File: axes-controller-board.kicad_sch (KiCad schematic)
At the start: 59 parts, among them IC1 TPS5450QDDARQ1, J10 Conn_01x08, J11 Conn_01x04, J12 Conn_01x08, J13 Conn_01x04, J14 Conn_01x08, J15 Conn_01x08, J16 Conn_01x04, J17 Conn_01x08, J18 Conn_01x08, J19 Conn_01x04, J2 Conn_01x03, J20 Conn_01x08, J21 Conn_01x08, J22 Conn_01x04, J23 Conn_01x08, J24 Conn_01x08, J25 Conn_01x04, J26 Conn_01x08, J27 Raspberry_Pi_2_3, J28 DC1, J29 DC2, J3 Conn_01x03, J30 DC3, J31 Conn_01x08, J32 Conn_01x08, J33 DC1, J4 Conn_01x03, J5 DRIVER, J6 NTC, J7 DRIVER, J8 NTC, J9 Conn_01x08, U1 LM1117MP-3.3

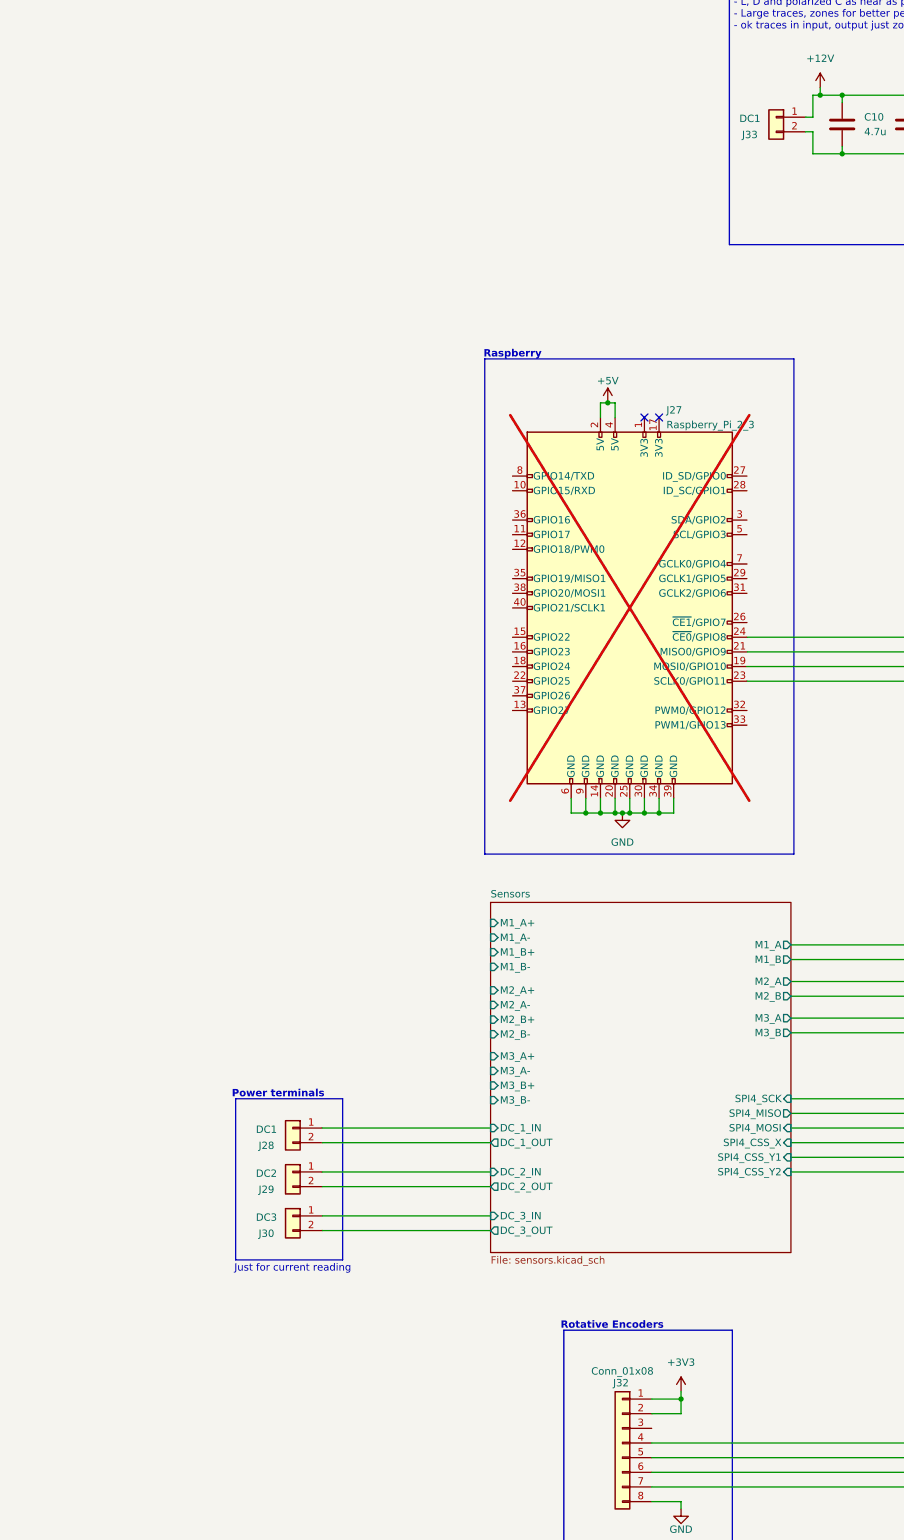
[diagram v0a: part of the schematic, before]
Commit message: fix: connectors and pcb layout
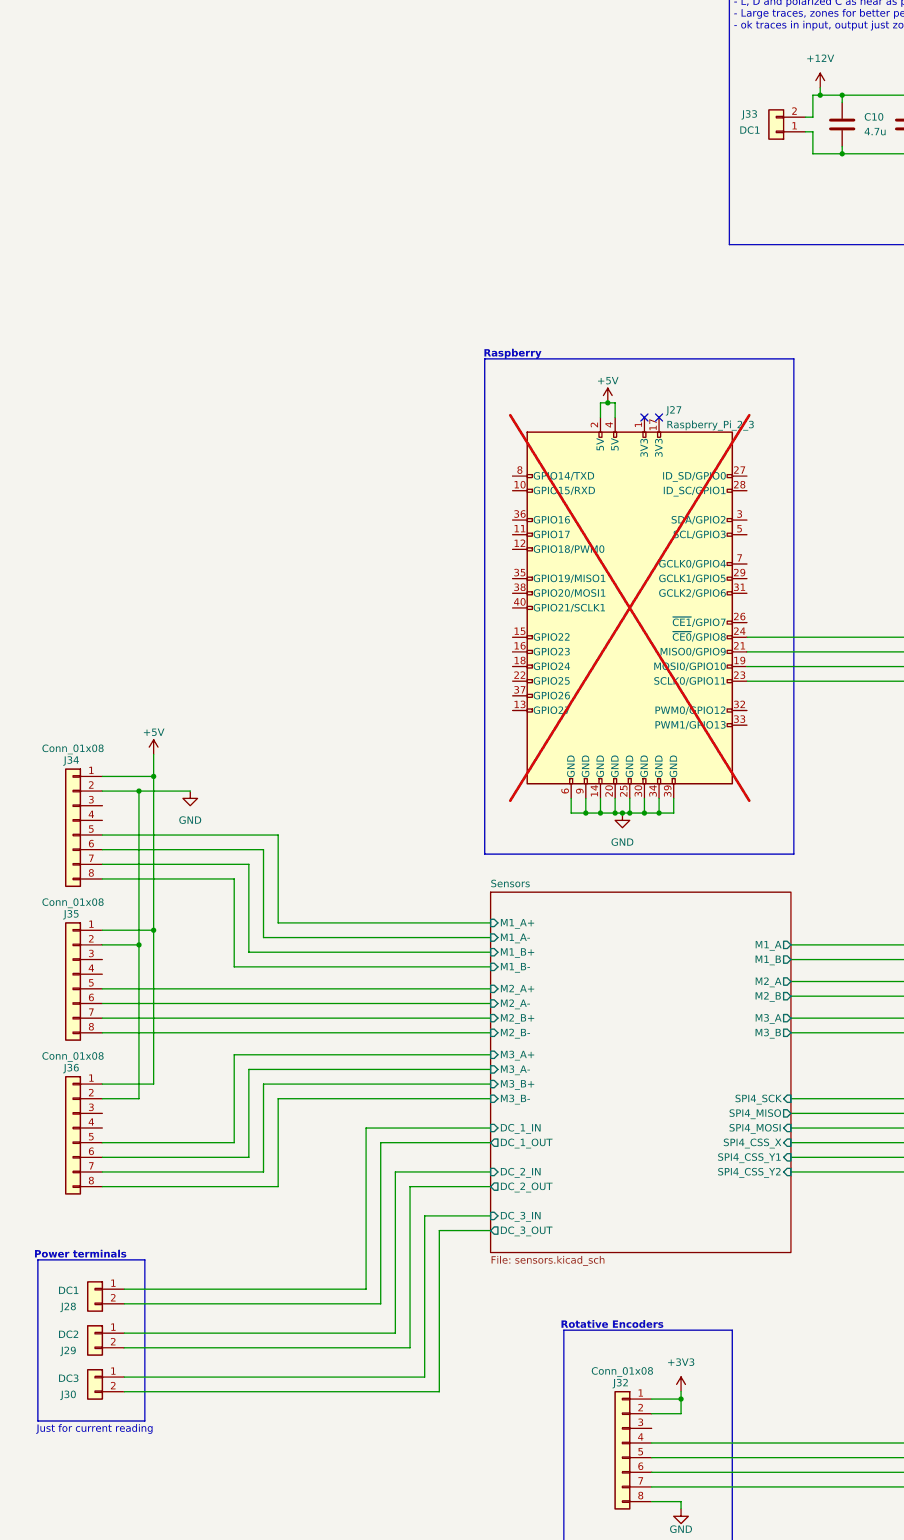
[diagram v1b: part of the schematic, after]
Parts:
- added J34, J35, J36: Conn_01x08, Local:1985250, symbol Connector_Generic:Conn_01x08
- J2, J3, J4: footprint Connector_PinHeader_2.54mm:PinHeader_1x03_P2.54mm_Vertical -> Local:1985205
- J31, J32: footprint Connector_Molex:Molex_Micro-Fit_3.0_43045-0812_2x04_P3.00mm_Vertical -> Local:1985250
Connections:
- net +12V: now also J33.2 (Pin_2); no longer J33.1 (Pin_1)
- net +5V: now also J34.1 (Pin_1), J35.1 (Pin_1), J36.1 (Pin_1)
- net GND: now also J33.1 (Pin_1), J34.2 (Pin_2), J35.2 (Pin_2), J36.2 (Pin_2); no longer J33.2 (Pin_2)
- net Sensors/M1_A+: now also J34.5 (Pin_5)
- net Sensors/M1_A-: now also J34.6 (Pin_6)
- net Sensors/M1_B+: now also J34.7 (Pin_7)
- net Sensors/M1_B-: now also J34.8 (Pin_8)
- net Sensors/M2_A+: now also J35.5 (Pin_5)
- net Sensors/M2_A-: now also J35.6 (Pin_6)
- net Sensors/M2_B+: now also J35.7 (Pin_7)
- net Sensors/M2_B-: now also J35.8 (Pin_8)
- net Sensors/M3_A+: now also J36.5 (Pin_5)
- net Sensors/M3_A-: now also J36.6 (Pin_6)
- net Sensors/M3_B+: now also J36.7 (Pin_7)
- net Sensors/M3_B-: now also J36.8 (Pin_8)
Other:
- moved on the sheet: J28, J29, J30, J33

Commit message: feat: endstops integration
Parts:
- added J37, J38, J39: ENDSTOP, Connector_PinHeader_2.54mm:PinHeader_1x02_P2.54mm_Vertical, symbol Connector_Generic:Conn_01x02
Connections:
- net GND: now also J37.1 (Pin_1), J38.1 (Pin_1), J39.1 (Pin_1)
- new net MCU/ES_X: J37.2 (Pin_2)
- new net MCU/ES_Y1: J38.2 (Pin_2)
- new net MCU/ES_Y2: J39.2 (Pin_2)
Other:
- sheet MCU ports: added ES_X, ES_Y1, ES_Y2; removed none

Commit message: fix: 33R resistors
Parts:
- C51, C52, C53, C54, C55, C56: now not fitted
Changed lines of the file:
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@@
 		(in_bom yes)
 		(on_board yes)
-		(dnp no)
+		(dnp yes)
 		(fields_autoplaced yes)
 		(property "Reference" "C51"
@@
 		(in_bom yes)
 		(on_board yes)
-		(dnp no)
+		(dnp yes)
 		(fields_autoplaced yes)
 		(property "Reference" "C52"
@@
 		(in_bom yes)
 		(on_board yes)
-		(dnp no)
+		(dnp yes)
 		(fields_autoplaced yes)
 		(property "Reference" "C53"
@@
 		(in_bom yes)
 		(on_board yes)
-		(dnp no)
+		(dnp yes)
 		(fields_autoplaced yes)
 		(property "Reference" "C54"
@@
 		(in_bom yes)
 		(on_board yes)
-		(dnp no)
+		(dnp yes)
 		(fields_autoplaced yes)
 		(property "Reference" "C56"
@@
 		(in_bom yes)
 		(on_board yes)
-		(dnp no)
+		(dnp yes)
 		(fields_autoplaced yes)
 		(property "Reference" "C55"

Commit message: feat: spi4 connections
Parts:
- added J40: Conn_01x03, Local:1985205, symbol Connector_Generic:Conn_01x03
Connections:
- net +12V: now also J40.2 (Pin_2), J40.3 (Pin_3)
- net GND: now also J40.1 (Pin_1)
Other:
- note added: "Fans"
- moved on the sheet: C1, C10, C11, C12, C13, C14, C15, C2, C3, D1, D2, D3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

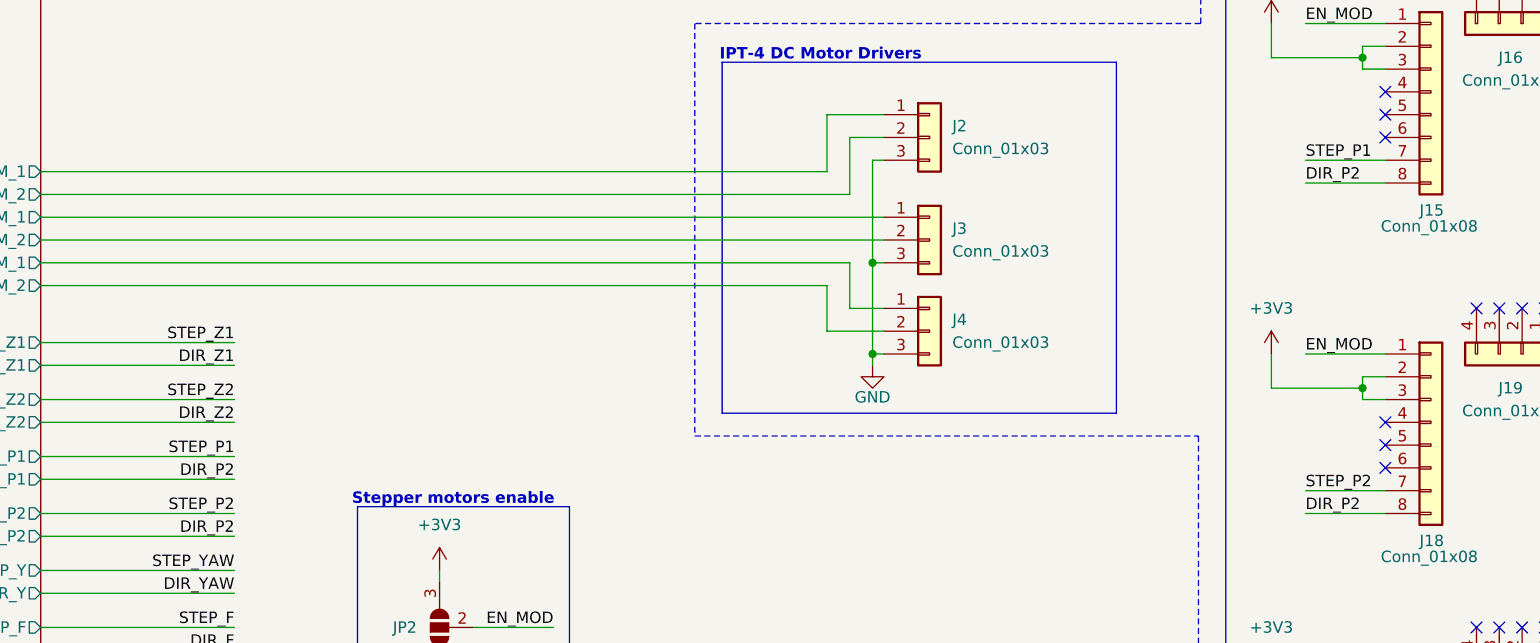
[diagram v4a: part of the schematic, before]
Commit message: feat: stepper motors connections to micro
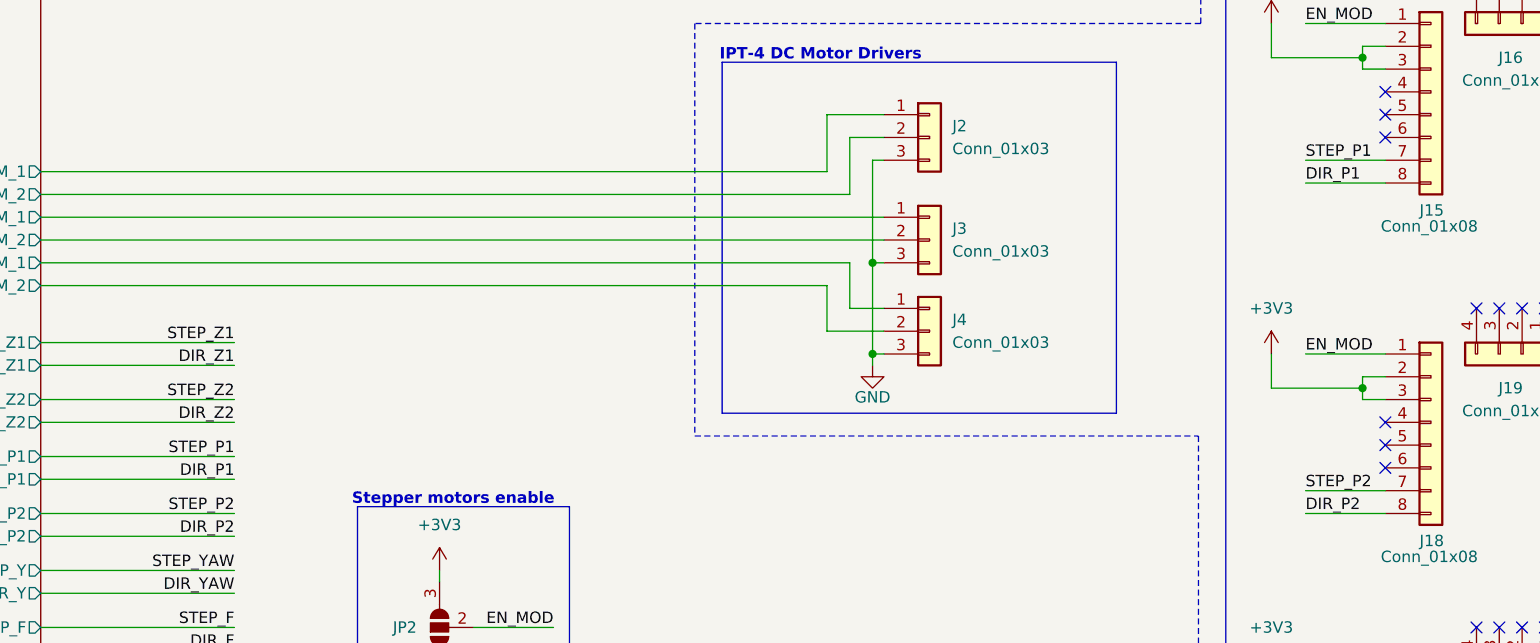
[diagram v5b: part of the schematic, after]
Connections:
- net DIR_P2: no longer J15.8 (Pin_8)
- new net DIR_P1: J15.8 (Pin_8)
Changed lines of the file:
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@@
 		)
 	)
-	(label "DIR_P2"
+	(label "DIR_P1"
 		(at 350.52 208.28 180)
 		(effects
@@
 		)
 	)
-	(label "DIR_P2"
+	(label "DIR_P1"
 		(at 469.9 175.26 0)
 		(effects

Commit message: fix: minors
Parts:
- added J41, J42: ENDSTOP, Connector_PinHeader_2.54mm:PinHeader_1x02_P2.54mm_Vertical, symbol Connector_Generic:Conn_01x02
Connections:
- net GND: now also J41.1 (Pin_1), J42.1 (Pin_1)
- new net MCU/ES_Z1: J41.2 (Pin_2)
- new net MCU/ES_Z2: J42.2 (Pin_2)
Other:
- sheet MCU ports: added ES_Z1, ES_Z2; removed none
- note added: "Endstops"
- moved on the sheet: C1, C10, C11, C12, C13, C14, C15, C2, C3, C51, C52, C53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

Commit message: fix: ground planes
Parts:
- added H1, H2: MountingHole_Pad, Local:TestPoint_GNDedge, symbol Mechanical:MountingHole_Pad
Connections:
- net GND: now also H1.1; no longer C51.2, C52.2, C53.2, C54.2, C55.2, C56.2, J10.2 (Pin_2), J14.2 (Pin_2), J17.2 (Pin_2), J20.2 (Pin_2), J23.2 (Pin_2), J26.2 (Pin_2)
- new net GNDM: C51.2, C52.2, C53.2, C54.2, C55.2, C56.2, H2.1, J10.2 (Pin_2), J14.2 (Pin_2), J17.2 (Pin_2), J20.2 (Pin_2), J23.2 (Pin_2), J26.2 (Pin_2)

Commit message: feat: nozzle and hb connections
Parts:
- added C41, C46: 100nF, Capacitor_SMD:C_0603_1608Metric, symbol Device:C
- added R33, R34: 10k, Resistor_SMD:R_0603_1608Metric, symbol Device:R
- added R41, R42: 1k, Resistor_SMD:R_0603_1608Metric, symbol Device:R
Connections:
- net +3V3: now also J6.3 (Pin_3), J8.3 (Pin_3), R33.2, R34.2
- net GND: now also J5.2 (Pin_2), J6.1 (Pin_1), J7.2 (Pin_2), J8.1 (Pin_1), C41.2, C46.2
- net H_PWM: now reaches J5.1 (Pin_1)
- net at J6.2 (Pin_2): now also R33.1, R41.2
- net at J8.2 (Pin_2): now also R34.1, R42.2
- net N_PWM: now reaches J7.1 (Pin_1)
- new net H_NTC: C41.1, R41.1
- new net N_NTC: C46.1, R42.1
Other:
- sheet MCU ports: added H_NTC, H_PWM, N_NTC, N_PWM; removed none
- moved on the sheet: J5, J6, J7
